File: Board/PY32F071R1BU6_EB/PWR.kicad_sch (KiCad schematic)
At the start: 14 parts, among them J1 USB_C_Receptacle_USB2.0_16P, U2 LTH7R/J, U3 XC6206P332MR-MS

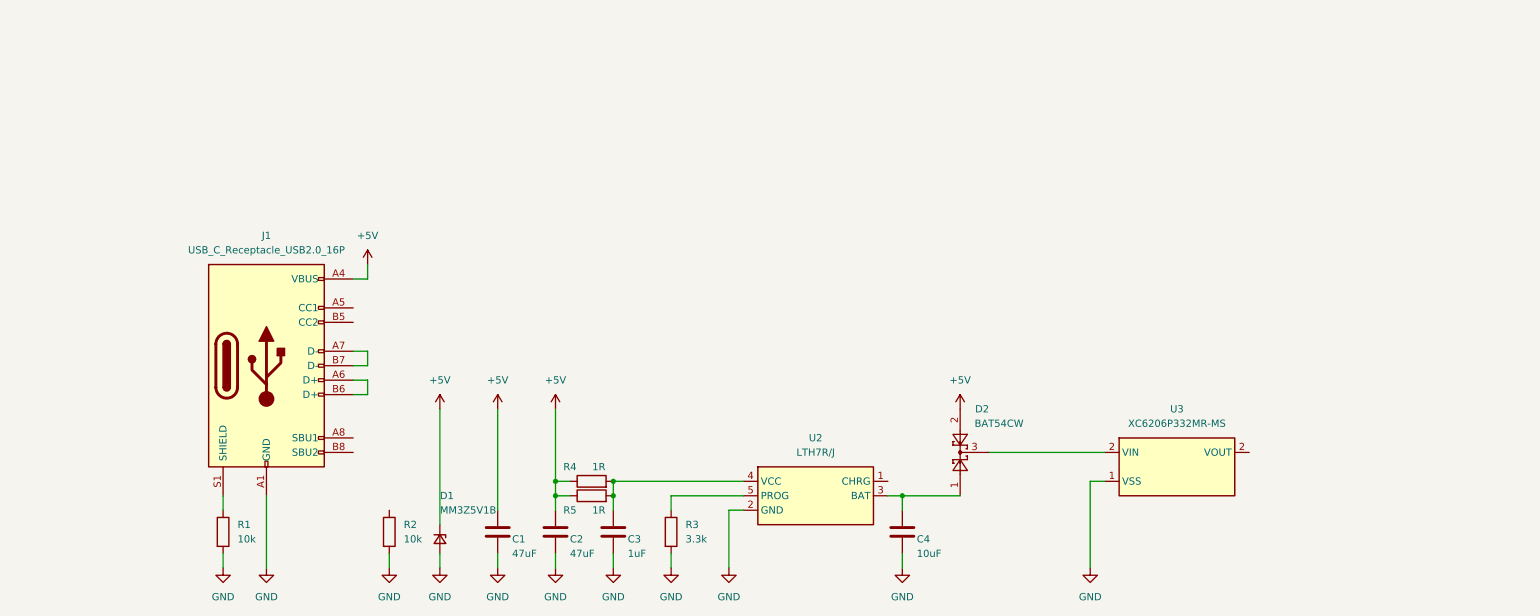
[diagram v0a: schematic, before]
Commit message: Power circuit prepared
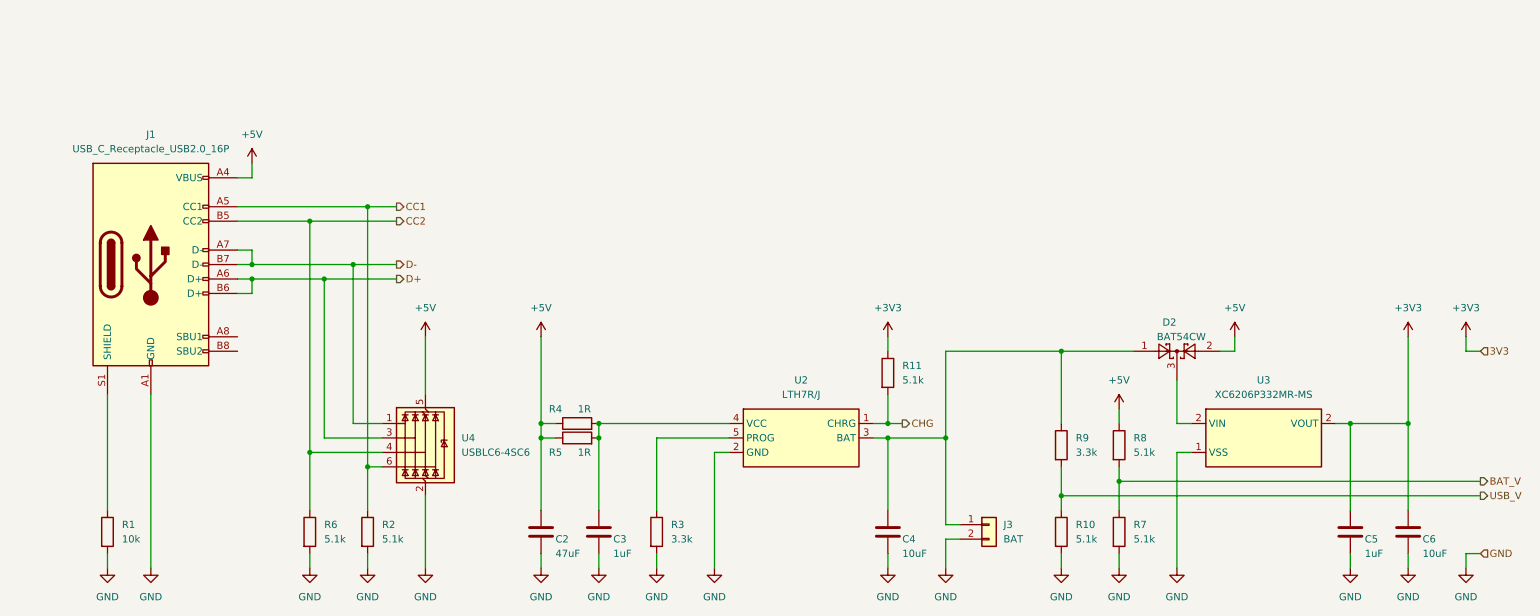
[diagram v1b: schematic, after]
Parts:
- removed C1: 47uF, Capacitor_SMD:C_0805_2012Metric_Pad1.18x1.45mm_HandSolder, symbol Device:C
- removed D1: MM3Z5V1B, Diode_SMD:D_SOD-323, symbol Device:D_Zener_Small
- added C5: 1uF, Capacitor_SMD:C_0603_1608Metric_Pad1.08x0.95mm_HandSolder, symbol Device:C
- added C6: 10uF, Capacitor_SMD:C_0603_1608Metric_Pad1.08x0.95mm_HandSolder, symbol Device:C
- added J3: BAT, Connector_PinHeader_2.54mm:PinHeader_1x02_P2.54mm_Horizontal, symbol Connector_Generic:Conn_01x02
- added R10, R11, R6, R7, R8: 5.1k, Resistor_SMD:R_0603_1608Metric_Pad0.98x0.95mm_HandSolder, symbol Device:R
- added R9: 3.3k, Resistor_SMD:R_0603_1608Metric_Pad0.98x0.95mm_HandSolder, symbol Device:R
- added U4: USBLC6-4SC6, Package_TO_SOT_SMD:SOT-23-6, symbol Power_Protection:USBLC6-4SC6
- R2: value 10k -> 5.1k
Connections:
- net +5V: now also R8.1, U4.5 (VBUS)
- net GND: now also C5.2, C6.2, J3.2 (Pin_2), R10.2, R6.2, R7.2, U4.2 (GND)
- net CC1: now reaches J1.A5 (CC1)
- net CC1: now also R2.1, U4.6 (I/O4)
- net D+: now reaches J1.A6 (D+), J1.B6 (D+)
- net D+: now also U4.3 (I/O2)
- net D-: now reaches J1.A7 (D-), J1.B7 (D-)
- net D-: now also U4.1 (I/O1)
- net CC2: now reaches J1.B5 (CC2)
- net CC2: now also R6.1, U4.4 (I/O3)
- net at C4.1, D2.1, U2.3 (BAT): now also J3.1 (Pin_1), R9.1
- net CHG: now reaches U2.1 (CHRG)
- net CHG: now also R11.2
- net +3V3: now reaches U3.2 (VOUT)
- net +3V3: now also C5.1, C6.1, R11.1
- new net BAT_V: R7.1, R8.2
- new net USB_V: R10.1, R9.2
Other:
- moved on the sheet: C2, C3, C4, D2, J1, R1, R2, R3, R4, R5, U2, U3

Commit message: Component placement started
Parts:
- removed D2: BAT54CW, Package_TO_SOT_SMD:SOT-323_SC-70, symbol Diode:BAT54CW
- added C10: 1uF, Capacitor_SMD:C_0603_1608Metric_Pad1.08x0.95mm_HandSolder, symbol Device:C
- added C11: 10uF, Capacitor_SMD:C_0603_1608Metric_Pad1.08x0.95mm_HandSolder, symbol Device:C
- added D6: BAT54C, Package_TO_SOT_SMD:SOT-23-3, symbol Diode:BAT54C
- added U6: XC6206P182MR-MS, Package_TO_SOT_SMD:SOT-23-3, symbol USER:XC6206P182MR-MS
- J3: footprint Connector_PinHeader_2.54mm:PinHeader_1x02_P2.54mm_Horizontal -> Connector_PinHeader_2.54mm:PinHeader_1x02_P2.54mm_Vertical
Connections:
- net +5V: now also D6.1
- net BAT_V: now also R10.1, R9.2; no longer R7.1, R8.2
- net GND: now also C10.2, C11.2, U6.1 (VSS)
- net USB_V: now also R7.1, R8.2; no longer R10.1, R9.2
- net at C4.1, J3.1 (Pin_1), R9.1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: now also D6.2
- new net: C11.1, D6.3, U3.3 (VIN), U6.3 (VIN)
- new net +1V8: C10.1, U6.2 (VOUT)
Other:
- moved on the sheet: C2, C3, C4, C5, C6, J1, J3, R1, R10, R11, R2, R3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
